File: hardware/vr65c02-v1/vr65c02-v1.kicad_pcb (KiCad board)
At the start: 2 copper layers, 7 parts, among them J1 Conn_01x06, J2 Conn_01x06, U1 ATMEGA4809, U2 W65C02

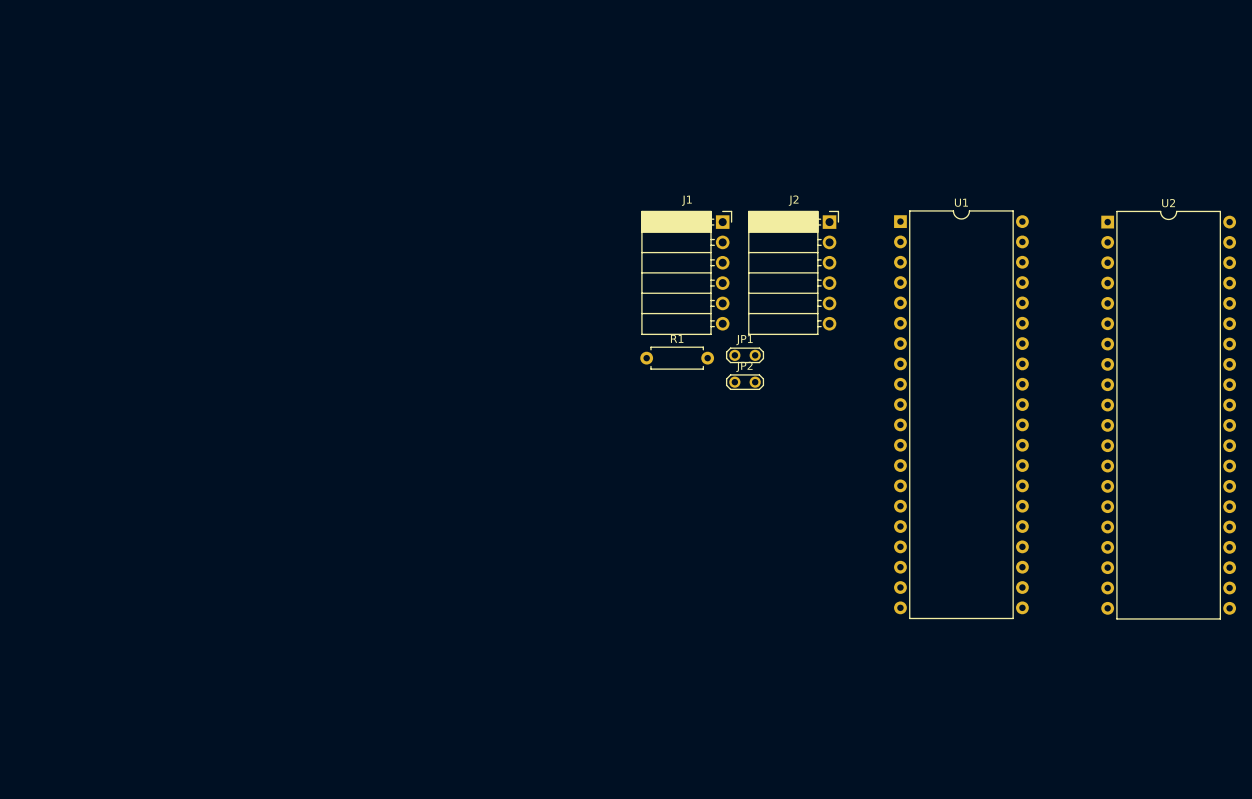
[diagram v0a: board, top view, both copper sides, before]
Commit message: PCB v1 routed
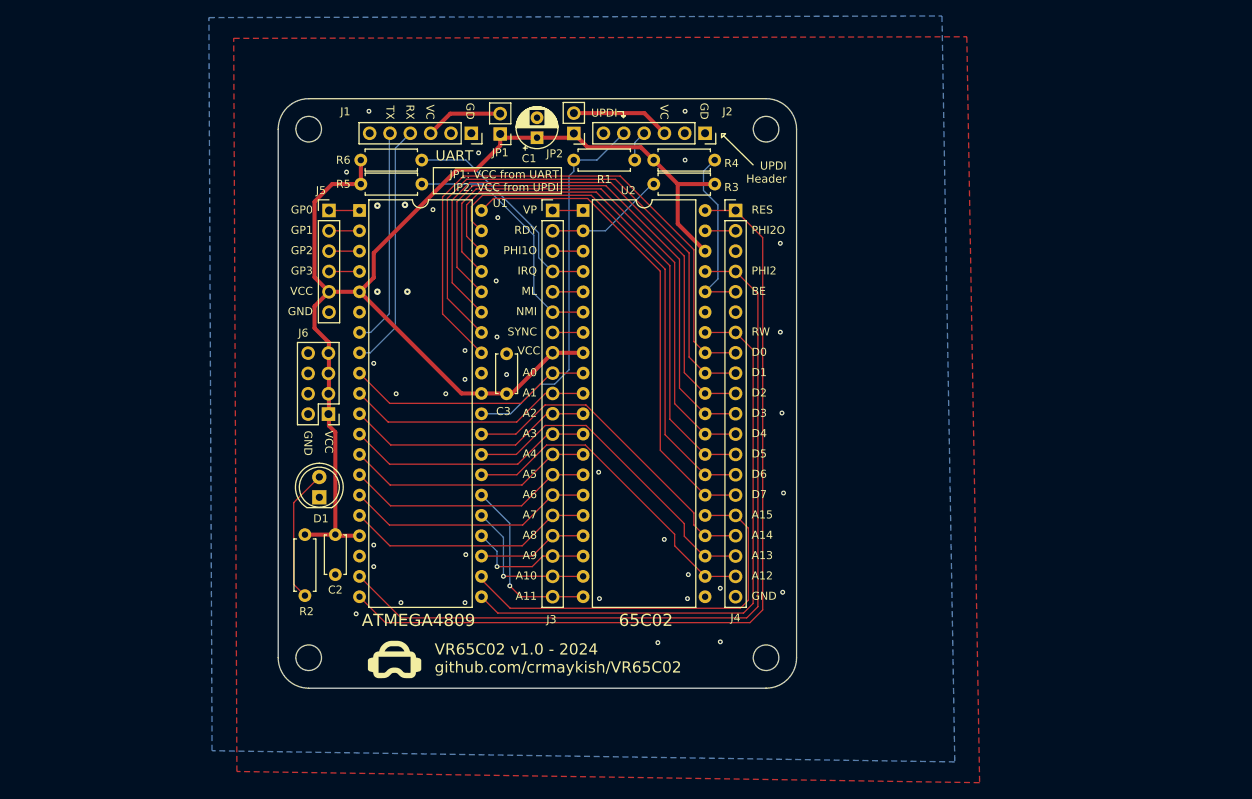
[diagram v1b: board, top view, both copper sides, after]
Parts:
- added C1: 10u, Capacitor_THT:CP_Radial_D5.0mm_P2.50mm, F.Cu at (55.2, 29.0)
- added C2: 0.1u, Capacitor_THT:C_Disc_D4.7mm_W2.5mm_P5.00mm, F.Cu at (30.0, 78.6)
- added C3: 0.1u, Capacitor_THT:C_Disc_D4.7mm_W2.5mm_P5.00mm, F.Cu at (51.4, 61.0)
- added D1: LED, LED_THT:LED_D5.0mm, F.Cu at (28.0, 73.9)
- added G***: LOGO, LOGO, F.Cu at (37.4, 94.2)
- added H1: MountingHole, MountingHole:MountingHole_3.2mm_M3, F.Cu at (26.7, 27.9)
- added H2: MountingHole, MountingHole:MountingHole_3.2mm_M3, F.Cu at (83.8, 27.9)
- added H3: MountingHole, MountingHole:MountingHole_3.2mm_M3, F.Cu at (26.7, 94.0)
- added H4: MountingHole, MountingHole:MountingHole_3.2mm_M3, F.Cu at (83.8, 94.0)
- added J3: Conn_01x20, Connector_PinHeader_2.54mm:PinHeader_1x20_P2.54mm_Vertical, F.Cu at (57.1, 38.1)
- added J4: Conn_01x20, Connector_PinHeader_2.54mm:PinHeader_1x20_P2.54mm_Vertical, F.Cu at (80.0, 38.1)
- added J5: Conn_01x06, Connector_PinHeader_2.54mm:PinHeader_1x06_P2.54mm_Vertical, F.Cu at (29.2, 38.1)
- added J6: Conn_02x04_Odd_Even, Connector_PinHeader_2.54mm:PinHeader_2x04_P2.54mm_Vertical, F.Cu at (29.1, 63.5)
- added R2: 470, Resistor_THT:R_Axial_DIN0207_L6.3mm_D2.5mm_P7.62mm_Horizontal, F.Cu at (26.2, 86.2)
- added R3: 4k7, Resistor_THT:R_Axial_DIN0207_L6.3mm_D2.5mm_P7.62mm_Horizontal, F.Cu at (69.8, 34.8)
- added R4: 4k7, Resistor_THT:R_Axial_DIN0207_L6.3mm_D2.5mm_P7.62mm_Horizontal, F.Cu at (77.4, 31.8)
- added R5: 4k7, Resistor_THT:R_Axial_DIN0207_L6.3mm_D2.5mm_P7.62mm_Horizontal, F.Cu at (40.8, 34.8)
- added R6: 4k7, Resistor_THT:R_Axial_DIN0207_L6.3mm_D2.5mm_P7.62mm_Horizontal, F.Cu at (40.8, 31.8)
- J1, J2: footprint Connector_PinSocket_2.54mm:PinSocket_1x06_P2.54mm_Horizontal -> Connector_PinSocket_2.54mm:PinSocket_1x06_P2.54mm_Vertical
- JP1, JP2: footprint TestPoint:TestPoint_2Pads_Pitch2.54mm_Drill0.8mm -> Connector_PinHeader_2.54mm:PinHeader_1x02_P2.54mm_Vertical
- moved U1 67.6 mm to (33.0, 38.1)
- moved U2 65.6 mm to (61.0, 38.1)
- moved JP1 40.3 mm to (50.6, 28.5), turned to 180 degrees
- moved JP2 37.0 mm to (59.8, 28.5), turned to 180 degrees
- moved J1 33.3 mm to (47.0, 28.4), turned to -90 degrees
- moved R1 26.4 mm to (59.8, 31.8)
- moved J2 19.1 mm to (76.2, 28.4), turned to -90 degrees
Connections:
- net A0 renamed /A0
- net A1 renamed /A1
- net A10 renamed /A10
- net A11 renamed /A11
- net A12 renamed /A12
- net A13 renamed /A13
- net A14 renamed /A14
- net A15 renamed /A15
- net A2 renamed /A2
- net A3 renamed /A3
- net A4 renamed /A4
- net A5 renamed /A5
- net A6 renamed /A6
- net A7 renamed /A7
- net A8 renamed /A8
- net A9 renamed /A9
- net D0 renamed /D0
- net D1 renamed /D1
- net D2 renamed /D2
- net D3 renamed /D3
- net D4 renamed /D4
- net D5 renamed /D5
- net D6 renamed /D6
- net D7 renamed /D7
- net /RW renamed /RW
- J1 pad 4: RX -> /RX
- J1 pad 5: TX -> /TX
- J2 pad 4: UPDI -> Net-(J2-Pin_4)
- J2 pad 5: Net-(J2-Pin_5) -> UPDI
- R1 pad 2: Net-(J2-Pin_5) -> Net-(J2-Pin_4)
- U1 pad 1: TX -> /GP0
- U1 pad 19: /RES -> /PHI2
- U1 pad 2: RX -> /GP1
- U1 pad 20: CLK -> /RES
- U1 pad 3: unconnected-(U1-PC2-Pad3) -> /GP2
- U1 pad 4: unconnected-(U1-PC3-Pad4) -> /GP3
- U1 pad 7: unconnected-(U1-PC4-Pad7) -> /TX
- U1 pad 8: unconnected-(U1-PC5-Pad8) -> /RX
- U2 pad 1: unconnected-(U2-/VP-Pad1) -> /VP
- U2 pad 2: RDY -> /RDY
- U2 pad 3: unconnected-(U2-PHI1O-Pad3) -> /PHI1O
- U2 pad 36: BE -> /BE
- U2 pad 37: CLK -> /PHI2
- U2 pad 38: unconnected-(U2-/SO-Pad38) -> +5V
- U2 pad 39: unconnected-(U2-PHI2O-Pad39) -> /PHI2O
- U2 pad 4: unconnected-(U2-/IRQ-Pad4) -> /IRQ
- U2 pad 40: /RES -> /RES
- U2 pad 5: unconnected-(U2-/ML-Pad5) -> /ML
- U2 pad 6: unconnected-(U2-/NMI-Pad6) -> /NMI
- U2 pad 7: unconnected-(U2-SYNC-Pad7) -> /SYNC
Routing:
- net +5V: track 0.00 -> 168.0 mm
- net /RES: track 0.00 -> 107.5 mm
- net /PHI2: track 0.00 -> 99.4 mm
- net /D0: track 0.00 -> 75.1 mm
- net /RW: track 0.00 -> 73.9 mm
- net /D1: track 0.00 -> 73.2 mm
- net /D2: track 0.00 -> 71.3 mm
- net /D3: track 0.00 -> 69.4 mm
- net /D4: track 0.00 -> 67.5 mm
- net /D5: track 0.00 -> 65.6 mm
- net /D6: track 0.00 -> 63.7 mm
- net /D7: track 0.00 -> 60.8 mm
- net /A15: track 0.00 -> 50.7 mm
- net UPDI: track 0.00 -> 47.3 mm
- net /A12: track 0.00 -> 40.9 mm
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- added copper zone on B.Cu, net GND
- added copper zone on F.Cu, net GND
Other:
- board outline added: 64.8 x 73.7 mm
- board text added: "65C02"
- board text added: "A0"
- board text added: "A1"
- board text added: "A10"
- board text added: "A11"
- board text added: "A12"
- board text added: "A13"
- board text added: "A14"
- board text added: "A15"
- board text added: "A2"
- board text added: "A3"
- board text added: "A4"
- board text added: "A5"
- board text added: "A6"
- board text added: "A7"
- board text added: "A8"
- board text added: "A9"
- board text added: "ATMEGA4809"
- board text added: "BE"
- board text added: "D0"
- board text added: "D1"
- board text added: "D2"
- board text added: "D3"
- board text added: "D4"
- board text added: "D5"
- board text added: "D6"
- board text added: "D7"
- board text added: "GD"
- board text added: "GND"
- board text added: "GP0"
- board text added: "GP1"
- board text added: "GP2"
- board text added: "GP3"
- board text added: "IRQ"
- board text added: "JP1: VCC from UART JP2: VCC from UPDI"
- board text added: "ML"
- board text added: "NMI"
- board text added: "PHI1O"
- board text added: "PHI2"
- board text added: "PHI2O"
- board text added: "RDY"
- board text added: "RES"
- board text added: "RW"
- board text added: "RX"
- board text added: "SYNC"
- board text added: "TX"
- board text added: "UART"
- board text added: "UPDI"
- board text added: "UPDI Header"
- board text added: "VC"
- board text added: "VCC"
- board text added: "VP"
- board text added: "VR65C02 v1.0 - 2024 github.com/crmaykish/VR65C02"

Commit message: Basic soft reset button option
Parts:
- added R7: 10k, Resistor_THT:R_Axial_DIN0207_L6.3mm_D2.5mm_P7.62mm_Horizontal, F.Cu at (-3.95, 35.0)
- added SW1: SW_Push, Button_Switch_THT:SW_PUSH_6mm_H5mm, F.Cu at (-8.90, 43.4)

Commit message: PCB release v1.0a
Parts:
- moved R7 78.2 mm to (49.9, 91.6), turned to 180 degrees
- moved SW1 71.2 mm to (39.4, 95.7), turned to 180 degrees
- moved G*** 38.9 mm to (76.3, 94.1)
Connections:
- R7 pad 1: /SOFT_RES -> /GP0
- SW1 pad 2: /SOFT_RES -> /GP0
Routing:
- net /GP0: track 3.81 -> 101.9 mm
- net +5V: track 168.0 -> 192.7 mm
- net GND: vias 38 -> 40
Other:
- board text added: "GP2=SDA GP3=SCL"
- board text added: "RESET"
- board text added: "VR65C02 v1.0 - 2024"
- board text added: "github.com/crmaykish/VR65C02"
- board text removed: "VR65C02 v1.0 - 2024 github.com/crmaykish/VR65C02"
